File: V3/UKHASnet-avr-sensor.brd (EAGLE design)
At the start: 49.5 x 49.2 mm, 26 parts, among them J1 AVR_SPI_PRG_62X3_LOCK, U1 MCP1700-3302E/TO, U2 ATMEGA328P-PU, X2 SMA-142-0711-821/826, Y1 RESONATORPTH

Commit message: Add final V3 files.
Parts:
- removed JP1: M02PTH, SparkFun-Connectors:1X02
- removed U$3: (no value), SparkFun-Aesthetics:OSHW-LOGO-M
- added JP7: M02JST-PTH-VERT, SparkFun-Connectors:JST-2-PTH-VERT
- moved JP6 7.68 mm to (22.6, 1.59), turned to 180 degrees
- moved R2 0.64 mm to (31.8, 19.1)
- moved R1 0.64 mm to (27.9, 19.1)
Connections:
- net GND: now also JP6.1, JP6.2, JP7.1; no longer JP1.1, JP6.3, JP6.4
- net SENSE1: now also JP6.3; no longer JP6.2
- net SENSE_VCC: now also JP6.4; no longer JP6.1
- net VIN: now also JP7.2; no longer JP1.2
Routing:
- net VIN: track 24.2 -> 21.9 mm
- net BATT_ADC: track 19.2 -> 19.9 mm
- net MOSI: track 55.4 -> 56.0 mm
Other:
- board text added: "/home/phil/Dropbox/Shared/Icons/4.bmp"

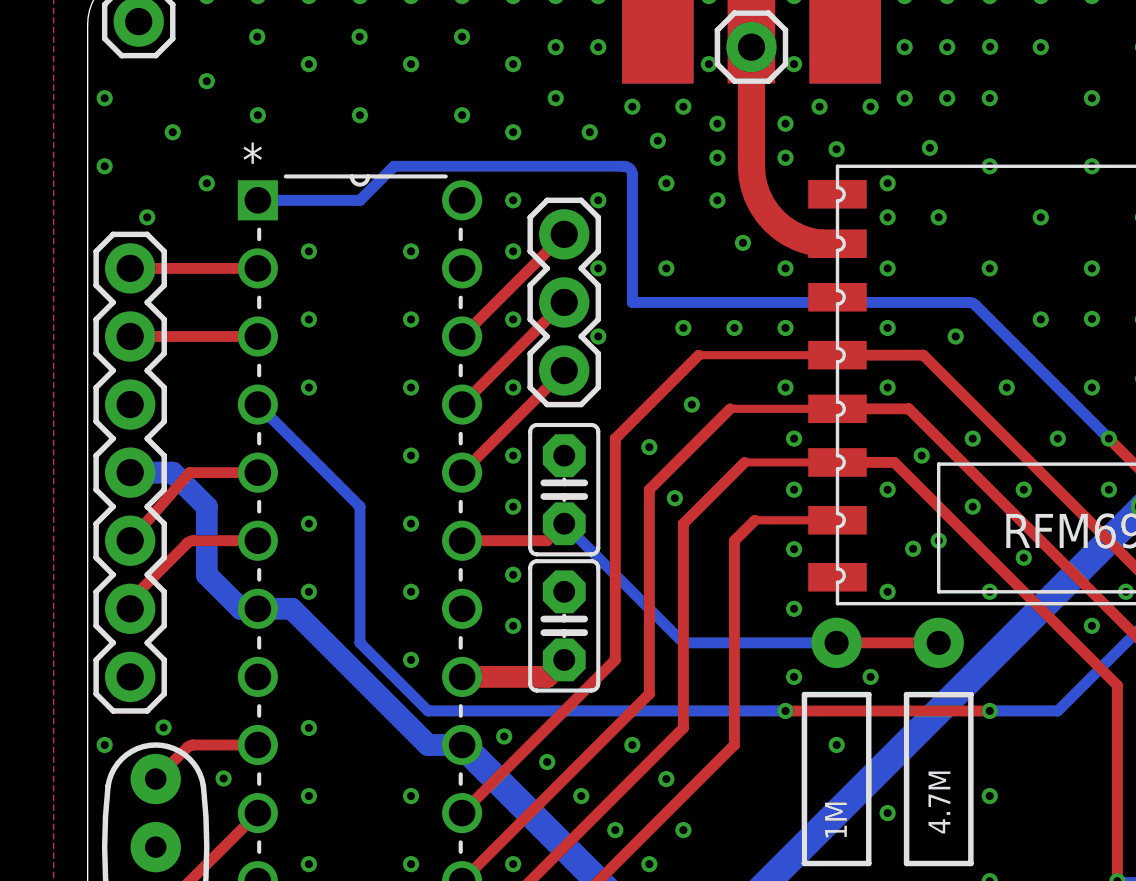
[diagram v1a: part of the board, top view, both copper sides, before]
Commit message: Move GPIO headers to line up. (0.1")
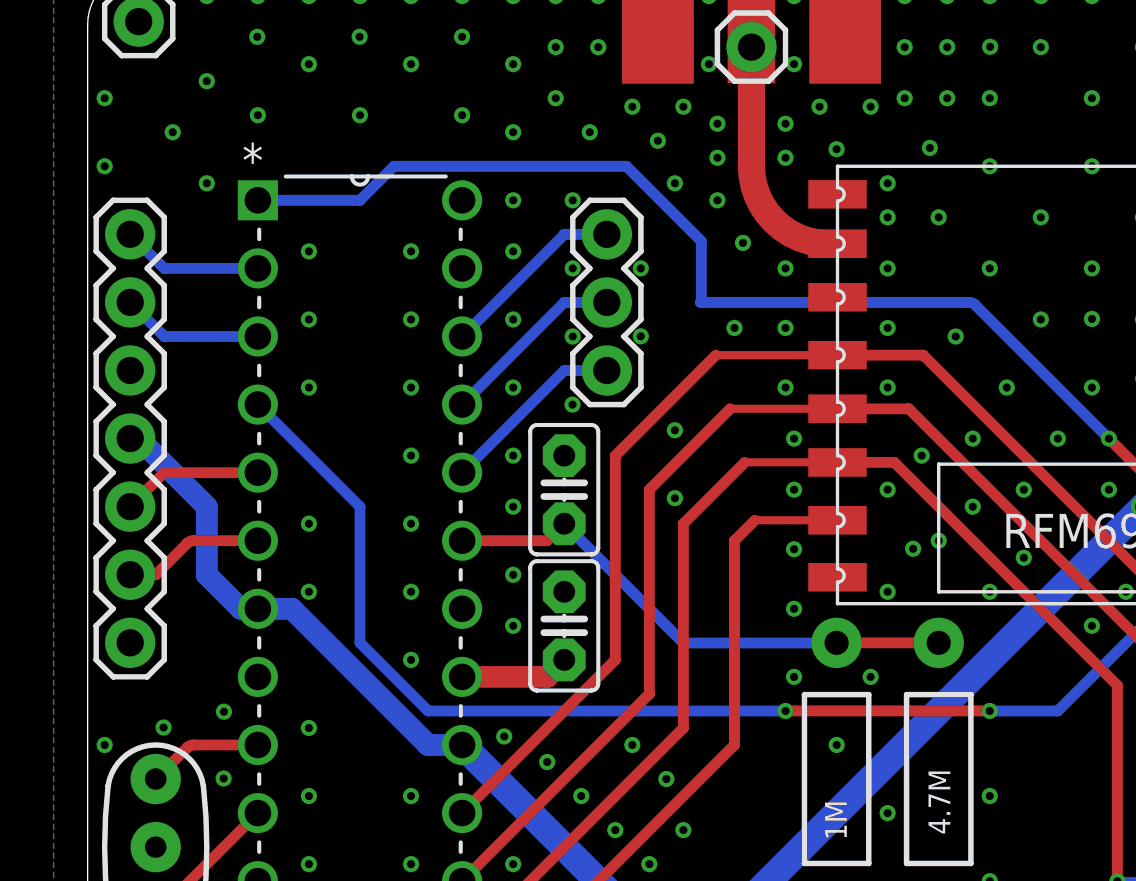
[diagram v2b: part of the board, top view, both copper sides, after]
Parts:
- moved JP5 1.59 mm to (19.4, 34.3)
- moved JP16 1.27 mm to (1.59, 39.4)
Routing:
- net ADC3: track 5.39 -> 6.98 mm
- net ADC2: track 5.39 -> 6.98 mm
- net ADC1: track 5.39 -> 6.98 mm
- net RST: track 68.6 -> 67.2 mm
- net D3: track 5.92 -> 5.29 mm
- net UART_TX: track 4.76 -> 5.29 mm
- net UART_RX: track 4.76 -> 5.29 mm
- net VCC: track 112.8 -> 113.4 mm
